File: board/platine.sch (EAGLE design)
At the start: 6 parts, among them T1 BC846, T2 BC846

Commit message: added latest schematic
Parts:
- added C1: 100n, rcl:C-EUC1206
- added F1, F2, F3: FUSESHK20L, fuse:FUSESHK20L
- added R5: 39k, rcl:R-EU_M1206
- added R6: 2k, rcl:R-EU_M1206
- added R7: 3k, rcl:R-EU_M1206
- added SV1: (no value), con-lstb:MA13-2
- added U$1: MAX7301AAX+, maxim:MAX7301AAX+
- added X1: (no value), con-subd:F15HPS
- added X10: (no value), con-berg:PN87520
- added X11, X15, X16, X17, X18: 22-23-2031, con-molex:22-23-2031
- added X12, X13, X14: (no value), con-wago:233-506
- added X2: (no value), con-subd:F09HPS
- added X3, X4, X5: 1751251, con-phoenix-350:1751251
- added X7, X8, X9: 1751248, con-phoenix-350:1751248
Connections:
- new net +5V: C1.1, SV1.2, U$1.V+, X12.B-1, X13.B-1, X14.B-1, X15-1.S, X16-1.S, X17-1.S, X18-1.S
- new net N$10: U$1.P7, X1-3.F
- new net N$11: U$1.P8, X1-5.F
- new net N$12: U$1.P9, X1-6.F
- new net N$13: U$1.P10, X1-7.F
- new net N$14: U$1.P11, X1-11.F
- new net N$15: U$1.P12, X2-1.F
- new net N$16: U$1.P13, X2-2.F
- new net N$17: U$1.P14, X2-3.F
- new net N$18: U$1.P15, X2-4.F
- new net N$19: U$1.P16, X2-5.F
- new net N$20: U$1.P17, X2-6.F
- new net N$21: U$1.P18, X2-7.F
- new net N$22: SV1.23, U$1.SCLK
- new net N$23: SV1.19, U$1.DIN
- new net N$24: R6.2, U$1.DOUT
- new net N$25: F3.2, X10.1, X11-1.S
- new net N$26: U$1.P19, X15-2.S
- new net N$27: R5.2, U$1.ISET
- new net N$28: U$1.P20, X16-2.S
- new net N$29: U$1.P21, X17-2.S
- new net N$30: U$1.P22, X18-2.S
- new net N$31: U$1.P23, X14.B-2
- new net N$32: U$1.P24, X14.B-3
- new net N$33: U$1.P25, X14.B-4
- new net N$34: U$1.P26, X13.B-2
- new net N$35: U$1.P27, X13.B-3
- new net N$36: U$1.P28, X13.B-4
- new net N$37: U$1.P29, X12.B-2
- new net N$38: U$1.P30, X12.B-3
- new net N$39: U$1.P31, X12.B-4
- new net N$4: R4.1, U$1.P5
- new net N$40: F1.1, X3-3.K
- new net N$42: X3-1.K, X3-2.K, X4-2.K, X4-3.K, X5-2.K, X5-3.K
- new net N$43: F2.1, X7-2.K
- new net N$44: X8-1.K
- new net N$45: X7-1.K, X8-2.K, X9-2.K
- new net N$5: SV1.5, U$1.CS
- new net N$6: R6.1, R7.2, SV1.21
- new net N$7: T1.C, X1-8.F
- new net N$8: U$1.P4, X1-4.F
- new net N$9: U$1.P6, X1-12.F
- net +24V: now also F1.2, X1-10.F, X1-9.F, X4-1.K, X5-1.K
- net GND: now also C1.2, R5.1, R7.1, U$1.GND, U$1.GND1, X1-1.F, X1-2.F, X10.4, X12.B-5, X12.B-6, X13.B-5, X13.B-6, X14.B-5, X14.B-6, X15-3.S, X16-3.S, X17-3.S, X18-3.S
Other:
- moved on the sheet: R1, R2, R3, R4, T1, T2

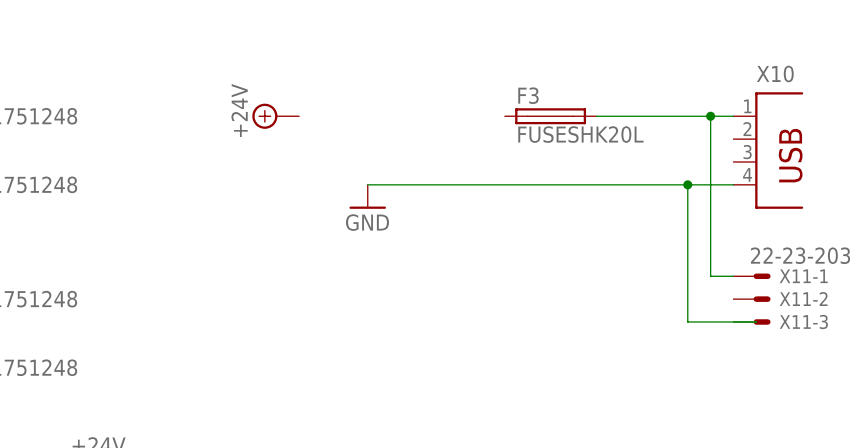
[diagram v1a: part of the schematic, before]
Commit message: added dc/dc converter
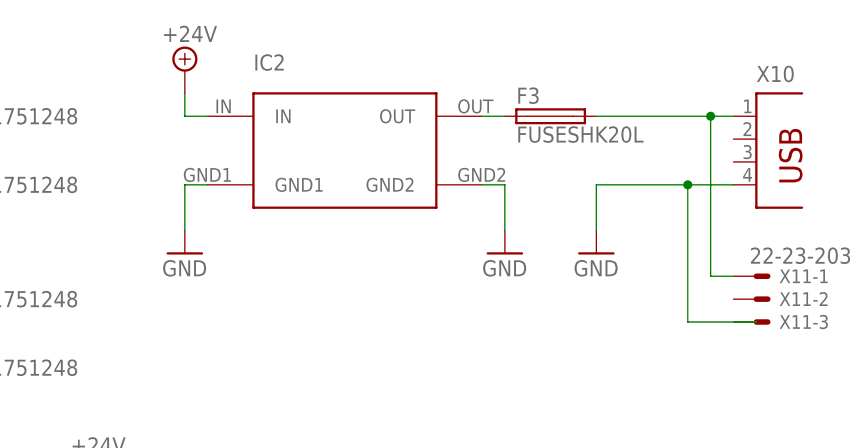
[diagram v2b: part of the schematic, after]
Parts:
- added IC2: SPS-1, sps-1:SPS-1
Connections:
- new net N$41: F3.1, IC2.OUT
- net +24V: now also IC2.IN
- net GND: now also IC2.GND1, IC2.GND2
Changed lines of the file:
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@@
 <grid distance="0.1" unitdist="inch" unit="inch" style="lines" multiple="1" display="no" altdistance="0.01" altunitdist="inch" altunit="inch"/>
 <layers>
-<layer number="1" name="Top" color="4" fill="1" visible="yes" active="no"/>
-<layer number="2" name="Route2" color="1" fill="3" visible="yes" active="no"/>
-<layer number="3" name="Route3" color="4" fill="3" visible="yes" active="no"/>
-<layer number="4" name="Route4" color="1" fill="4" visible="yes" active="no"/>
-<layer number="5" name="Route5" color="4" fill="4" visible="yes" active="no"/>
-<layer number="6" name="Route6" color="1" fill="8" visible="yes" active="no"/>
-<layer number="7" name="Route7" color="4" fill="8" visible="yes" active="no"/>
-<layer number="8" name="Route8" color="1" fill="2" visible="yes" active="no"/>
-<layer number="9" name="Route9" color="4" fill="2" visible="yes" active="no"/>
-<layer number="10" name="Route10" color="1" fill="7" visible="yes" active="no"/>
-<layer number="11" name="Route11" color="4" fill="7" visible="yes" active="no"/>
-<layer number="12" name="Route12" color="1" fill="5" visible="yes" active="no"/>
-<layer number="13" name="Route13" color="4" fill="5" visible="yes" active="no"/>
-<layer number="14" name="Route14" color="1" fill="6" visible="yes" active="no"/>
-<layer number="15" name="Route15" color="4" fill="6" visible="yes" active="no"/>
-<layer number="16" name="Bottom" color="1" fill="1" visible="yes" active="no"/>
-<layer number="17" name="Pads" color="2" fill="1" visible="yes" active="no"/>
-<layer number="18" name="Vias" color="2" fill="1" visible="yes" active="no"/>
-<layer number="19" name="Unrouted" color="6" fill="1" visible="yes" active="no"/>
-<layer number="20" name="Dimension" color="15" fill="1" visible="yes" active="no"/>
-<layer number="21" name="tPlace" color="7" fill="1" visible="yes" active="no"/>
-<layer number="22" name="bPlace" color="7" fill="1" visible="yes" active="no"/>
-<layer number="23" name="tOrigins" color="15" fill="1" visible="yes" active="no"/>
-<layer number="24" name="bOrigins" color="15" fill="1" visible="yes" active="no"/>
-<layer number="25" name="tNames" color="7" fill="1" visible="yes" active="no"/>
-<layer number="26" name="bNames" color="7" fill="1" visible="yes" active="no"/>
-<layer number="27" name="tValues" color="7" fill="1" visible="yes" active="no"/>
-<layer number="28" name="bValues" color="7" fill="1" visible="yes" active="no"/>
+<layer number="1" name="Top" color="4" fill="1" visible="no" active="no"/>
+<layer number="2" name="Route2" color="1" fill="3" visible="no" active="no"/>
+<layer number="3" name="Route3" color="4" fill="3" visible="no" active="no"/>
+<layer number="4" name="Route4" color="1" fill="4" visible="no" active="no"/>
+<layer number="5" name="Route5" color="4" fill="4" visible="no" active="no"/>
+<layer number="6" name="Route6" color="1" fill="8" visible="no" active="no"/>
+<layer number="7" name="Route7" color="4" fill="8" visible="no" active="no"/>
+<layer number="8" name="Route8" color="1" fill="2" visible="no" active="no"/>
+<layer number="9" name="Route9" color="4" fill="2" visible="no" active="no"/>
+<layer number="10" name="Route10" color="1" fill="7" visible="no" active="no"/>
+<layer number="11" name="Route11" color="4" fill="7" visible="no" active="no"/>
+<layer number="12" name="Route12" color="1" fill="5" visible="no" active="no"/>
+<layer number="13" name="Route13" color="4" fill="5" visible="no" active="no"/>
+<layer number="14" name="Route14" color="1" fill="6" visible="no" active="no"/>
+<layer number="15" name="Route15" color="4" fill="6" visible="no" active="no"/>
+<layer number="16" name="Bottom" color="1" fill="1" visible="no" active="no"/>
+<layer number="17" name="Pads" color="2" fill="1" visible="no" active="no"/>
+<layer number="18" name="Vias" color="2" fill="1" visible="no" active="no"/>
+<layer number="19" name="Unrouted" color="6" fill="1" visible="no" active="no"/>
+<layer number="20" name="Dimension" color="15" fill="1" visible="no" active="no"/>
+<layer number="21" name="tPlace" color="7" fill="1" visible="no" active="no"/>
+<layer number="22" name="bPlace" color="7" fill="1" visible="no" active="no"/>
+<layer number="23" name="tOrigins" color="15" fill="1" visible="no" active="no"/>
+<layer number="24" name="bOrigins" color="15" fill="1" visible="no" active="no"/>
+<layer number="25" name="tNames" color="7" fill="1" visible="no" active="no"/>
+<layer number="26" name="bNames" color="7" fill="1" visible="no" active="no"/>
+<layer number="27" name="tValues" color="7" fill="1" visible="no" active="no"/>
+<layer number="28" name="bValues" color="7" fill="1" visible="no" active="no"/>
 <layer number="29" name="tStop" color="7" fill="3" visible="no" active="no"/>
 <layer number="30" name="bStop" color="7" fill="6" visible="no" active="no"/>
@@
 <layer number="35" name="tGlue" color="7" fill="4" visible="no" active="no"/>
 <layer number="36" name="bGlue" color="7" fill="5" visible="no" active="no"/>
-<layer number="37" name="tTest" color="7" fill="1" visible="yes" active="no"/>
-<layer number="38" name="bTest" color="7" fill="1" visible="yes" active="no"/>
+<layer number="37" name="tTest" color="7" fill="1" visible="no" active="no"/>
+<layer number="38" name="bTest" color="7" fill="1" visible="no" active="no"/>
 <layer number="39" name="tKeepout" color="4" fill="11" visible="no" active="no"/>
 <layer number="40" name="bKeepout" color="1" fill="11" visible="no" active="no"/>
@@
 <layer number="44" name="Drills" color="7" fill="1" visible="no" active="no"/>
 <layer number="45" name="Holes" color="7" fill="1" visible="no" active="no"/>
-<layer number="46" name="Milling" color="3" fill="1" visible="yes" active="no"/>
-<layer number="47" name="Measures" color="7" fill="1" visible="yes" active="no"/>
-<layer number="48" name="Document" color="7" fill="1" visible="yes" active="no"/>
-<layer number="49" name="Reference" color="7" fill="1" visible="yes" active="no"/>
-<layer number="51" name="tDocu" color="6" fill="1" visible="yes" active="no"/>
-<layer number="52" name="bDocu" color="7" fill="1" visible="yes" active="no"/>
+<layer number="46" name="Milling" color="3" fill="1" visible="no" active="no"/>
+<layer number="47" name="Measures" color="7" fill="1" visible="no" active="no"/>
+<layer number="48" name="Document" color="7" fill="1" visible="no" active="no"/>
+<layer number="49" name="Reference" color="7" fill="1" visible="no" active="no"/>
+<layer number="51" name="tDocu" color="6" fill="1" visible="no" active="no"/>
+<layer number="52" name="bDocu" color="7" fill="1" visible="no" active="no"/>
 <layer number="91" name="Nets" color="2" fill="1" visible="yes" active="yes"/>
 <layer number="92" name="Busses" color="1" fill="1" visible="yes" active="yes"/>
@@
 <part name="GND14" library="supply1" deviceset="GND" device=""/>
 <part name="FRAME1" library="frames" deviceset="A3L-LOC" device=""/>
+<part name="IC2" library="sps-1" deviceset="SPS-1" device=""/>
+<part name="GND15" library="supply1" deviceset="GND" device=""/>
+<part name="GND16" library="supply1" deviceset="GND" device=""/>
 </parts>
 <sheets>
@@
 <instance part="SUPPLY10" gate="+5V" x="-10.16" y="139.7"/>
 <instance part="SUPPLY11" gate="+24V" x="-2.54" y="231.14"/>
-<instance part="SUPPLY12" gate="+24V" x="172.72" y="228.6" rot="R90"/>
-<instance part="GND14" gate="1" x="182.88" y="218.44"/>
+<instance part="SUPPLY12" gate="+24V" x="162.56" y="233.68"/>
+<instance part="GND14" gate="1" x="208.28" y="213.36"/>
 <instance part="FRAME1" gate="G$1" x="-96.52" y="-2.54"/>
+<instance part="IC2" gate="IC1" x="180.34" y="228.6"/>
+<instance part="GND15" gate="1" x="198.12" y="213.36"/>
+<instance part="GND16" gate="1" x="162.56" y="213.36"/>
 </instances>
 <busses>
@@
 <pinref part="GND14" gate="1" pin="GND"/>
 <pinref part="X10" gate="G$1" pin="4"/>
-<wire x1="182.88" y1="220.98" x2="218.44" y2="220.98" width="0.1524" layer="91"/>
+<wire x1="208.28" y1="215.9" x2="208.28" y2="220.98" width="0.1524" layer="91"/>
+<wire x1="208.28" y1="220.98" x2="218.44" y2="220.98" width="0.1524" layer="91"/>
 <wire x1="218.44" y1="220.98" x2="223.52" y2="220.98" width="0.1524" layer="91"/>
 <wire x1="226.06" y1="205.74" x2="218.44" y2="205.74" width="0.1524" layer="91"/>
 <wire x1="218.44" y1="205.74" x2="218.44" y2="220.98" width="0.1524" layer="91"/>
 <junction x="218.44" y="220.98"/>
+</segment>
+<segment>
+<pinref part="GND16" gate="1" pin="GND"/>
+<wire x1="162.56" y1="215.9" x2="162.56" y2="220.98" width="0.1524" layer="91"/>
+<pinref part="IC2" gate="IC1" pin="GND1"/>
+<wire x1="162.56" y1="220.98" x2="165.1" y2="220.98" width="0.1524" layer="91"/>
+</segment>
+<segment>
+<pinref part="GND15" gate="1" pin="GND"/>
+<wire x1="198.12" y1="215.9" x2="198.12" y2="220.98" width="0.1524" layer="91"/>
+<pinref part="IC2" gate="IC1" pin="GND2"/>
+<wire x1="198.12" y1="220.98" x2="195.58" y2="220.98" width="0.1524" layer="91"/>
 </segment>
 </net>
@@
 <pinref part="SUPPLY11" gate="+24V" pin="+24V"/>
 <junction x="-2.54" y="228.6"/>
+</segment>
+<segment>
+<pinref part="IC2" gate="IC1" pin="IN"/>
+<pinref part="SUPPLY12" gate="+24V" pin="+24V"/>
+<wire x1="162.56" y1="231.14" x2="162.56" y2="228.6" width="0.1524" layer="91"/>
+<wire x1="162.56" y1="228.6" x2="165.1" y2="228.6" width="0.1524" layer="91"/>
 </segment>
 </net>
@@
 </segment>
 </net>
+<net name="N$41" class="0">
+<segment>
+<pinref part="F3" gate="G$1" pin="1"/>
+<pinref part="IC2" gate="IC1" pin="OUT"/>
+<wire x1="195.58" y1="228.6" x2="198.12" y2="228.6" width="0.1524" layer="91"/>
+</segment>
+</net>

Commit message: New board
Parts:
- added C10, C2, C3, C4, C5, C6, C7, C8, C9: (no value), rcl:C-EUC1206
- added L1, L2, L3, L4: (no value), rcl:L-EUL0402
- added R8: 220K, rcl:R-EU_R0603
- C1: device rcl:C-EUC1206 -> rcl:C-EUC0603
- R1: value 10k -> 1K; device rcl:R-EU_M1206 -> rcl:R-EU_R0603
- R2, R3, R5, R6, R7: device rcl:R-EU_M1206 -> rcl:R-EU_R0603
- R4: value 3k -> 1K; device rcl:R-EU_M1206 -> rcl:R-EU_R0603
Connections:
- removed net N$25: F3.2, X10.1, X11-1.S
- new net N$46: L3.1, SV1.21
- new net N$47: L4.2, R6.1, R7.2
- net +24V: now also C4.2, C6.2, C7.2, C9.2
- net +5V: now also C2.2, C5.2, F3.2, X10.1, X11-1.S
- net GND: now also C10.1, C2.1, C3.1, C4.1, C5.1, C6.1, C7.1, C8.1, C9.1, R8.1, SV1.14, SV1.20, SV1.25, SV1.6, SV1.9, X11-3.S, X2-8.F, X2-9.F, X3-1.K, X3-2.K, X4-2.K, X4-3.K, X5-2.K, X5-3.K, X7-1.K, X8-2.K, X9-2.K
- net N$22: now also L2.2; no longer SV1.23
- net N$23: now also L3.2; no longer SV1.19
- net N$3: now also R8.2
- net N$41: now also C3.2
- net N$42: now also L1.1, SV1.24; no longer X3-1.K, X3-2.K, X4-2.K, X4-3.K, X5-2.K, X5-3.K
- net N$44: now also C10.2, C8.2, F2.2, X9-1.K
- net N$45: now also L2.1, SV1.23; no longer X7-1.K, X8-2.K, X9-2.K
- net N$5: now also L1.2; no longer SV1.5
- net N$6: now also L4.1, SV1.19; no longer R6.1, R7.2, SV1.21
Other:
- moved on the sheet: F2, X4-1, X4-2, X4-3
